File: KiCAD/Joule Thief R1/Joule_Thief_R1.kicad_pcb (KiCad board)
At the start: 2 copper layers, 95 x 62 mm, 35 parts, among them J2 Conn_01x06_Socket, Q1 AO3400A, Q2 AO3400A, SW1 SW_SPST, SW2 SW_SPST, U1 INA219AxD, U2 LTC3105xMS, U3 AD5280, U4 INA219AxD, U5 DW01A

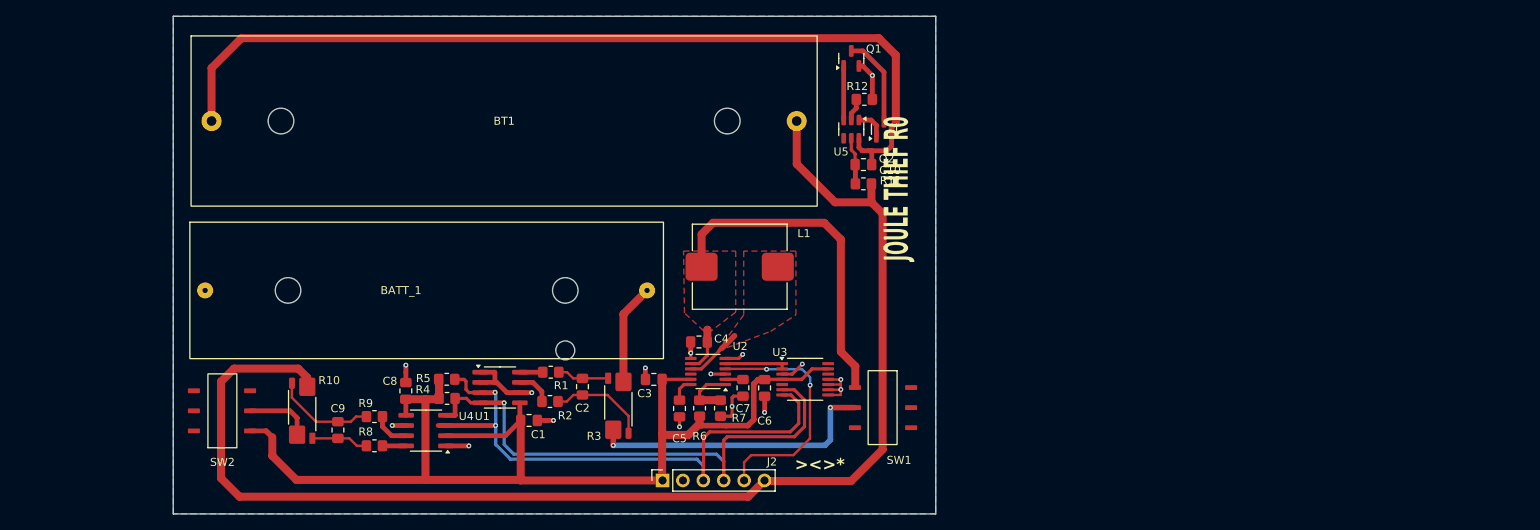
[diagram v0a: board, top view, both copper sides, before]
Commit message: layout extraction module
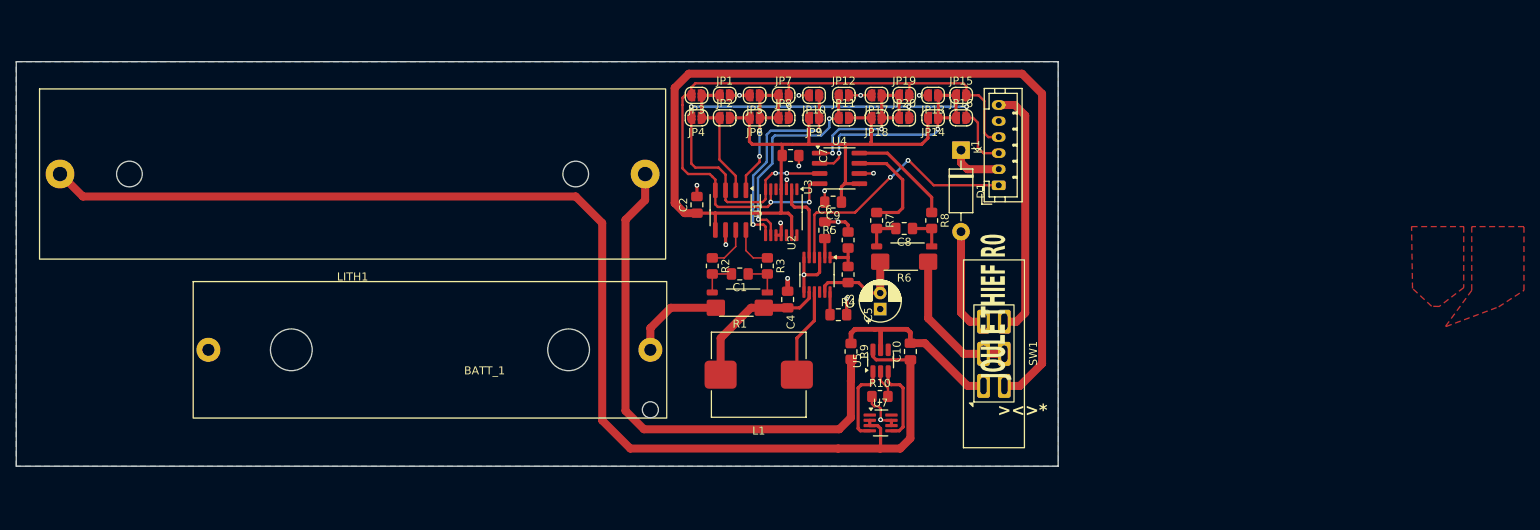
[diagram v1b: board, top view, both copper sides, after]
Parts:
- removed BT1: Battery_Cell, Joule Thief-Library:18650_Cell_Clip
- removed J2: Conn_01x06_Socket, Connector_PinSocket_2.54mm:PinSocket_1x06_P2.54mm_Vertical
- removed Q1, Q2: AO3400A, Package_TO_SOT_SMD:SOT-23
- removed R11: 100, Resistor_SMD:R_0805_2012Metric_Pad1.20x1.40mm_HandSolder
- removed R12: 1k, Resistor_SMD:R_0805_2012Metric_Pad1.20x1.40mm_HandSolder
- removed the R4 at (92.7, 77.0)
- removed the R5 at (92.7, 74.6)
- removed SW2: SW_SPST, Joule Thief-Library:SMD_DPST_Switch
- added D1: D_Schottky, Diode_THT:D_DO-41_SOD81_P10.16mm_Horizontal, F.Cu at (156.8, 46.0)
- added J1: Conn_01x06, Connector_JST:JST_PH_B6B-PH-K_1x06_P2.00mm_Vertical, F.Cu at (161.5, 50.4)
- added JP1: SolderJumper_2_Open, Jumper:SolderJumper-2_P1.3mm_Open_RoundedPad1.0x1.5mm, F.Cu at (127.3, 39.2)
- added JP10: SolderJumper_2_Open, Jumper:SolderJumper-2_P1.3mm_Open_RoundedPad1.0x1.5mm, F.Cu at (138.5, 39.2)
- added JP11: SolderJumper_2_Open, Jumper:SolderJumper-2_P1.3mm_Open_RoundedPad1.0x1.5mm, F.Cu at (142.2, 42.0)
- added JP12: SolderJumper_2_Open, Jumper:SolderJumper-2_P1.3mm_Open_RoundedPad1.0x1.5mm, F.Cu at (142.2, 39.2)
- added JP13: SolderJumper_2_Open, Jumper:SolderJumper-2_P1.3mm_Open_RoundedPad1.0x1.5mm, F.Cu at (153.3, 39.2)
- added JP14: SolderJumper_2_Open, Jumper:SolderJumper-2_P1.3mm_Open_RoundedPad1.0x1.5mm, F.Cu at (153.3, 42.0)
- added JP15: SolderJumper_2_Open, Jumper:SolderJumper-2_P1.3mm_Open_RoundedPad1.0x1.5mm, F.Cu at (156.8, 39.2)
- added JP16: SolderJumper_2_Open, Jumper:SolderJumper-2_P1.3mm_Open_RoundedPad1.0x1.5mm, F.Cu at (156.8, 42.0)
- added JP17: SolderJumper_2_Open, Jumper:SolderJumper-2_P1.3mm_Open_RoundedPad1.0x1.5mm, F.Cu at (146.2, 39.2)
- added JP18: SolderJumper_2_Open, Jumper:SolderJumper-2_P1.3mm_Open_RoundedPad1.0x1.5mm, F.Cu at (146.2, 42.0)
- added JP19: SolderJumper_2_Open, Jumper:SolderJumper-2_P1.3mm_Open_RoundedPad1.0x1.5mm, F.Cu at (149.7, 39.2)
- added JP2: SolderJumper_2_Open, Jumper:SolderJumper-2_P1.3mm_Open_RoundedPad1.0x1.5mm, F.Cu at (127.3, 42.0)
- added JP20: SolderJumper_2_Open, Jumper:SolderJumper-2_P1.3mm_Open_RoundedPad1.0x1.5mm, F.Cu at (149.7, 42.0)
- added JP3: SolderJumper_2_Open, Jumper:SolderJumper-2_P1.3mm_Open_RoundedPad1.0x1.5mm, F.Cu at (123.8, 39.2)
- added JP4: SolderJumper_2_Open, Jumper:SolderJumper-2_P1.3mm_Open_RoundedPad1.0x1.5mm, F.Cu at (123.8, 42.0)
- added JP5: SolderJumper_2_Open, Jumper:SolderJumper-2_P1.3mm_Open_RoundedPad1.0x1.5mm, F.Cu at (131.1, 39.2)
- added JP6: SolderJumper_2_Open, Jumper:SolderJumper-2_P1.3mm_Open_RoundedPad1.0x1.5mm, F.Cu at (131.1, 42.0)
- added JP7: SolderJumper_2_Open, Jumper:SolderJumper-2_P1.3mm_Open_RoundedPad1.0x1.5mm, F.Cu at (134.7, 39.2)
- added JP8: SolderJumper_2_Open, Jumper:SolderJumper-2_P1.3mm_Open_RoundedPad1.0x1.5mm, F.Cu at (134.7, 42.0)
- added JP9: SolderJumper_2_Open, Jumper:SolderJumper-2_P1.3mm_Open_RoundedPad1.0x1.5mm, F.Cu at (138.5, 42.0)
- added LITH1: 18650, 000_Dropbin:18650_Cell_Clip_V2, F.Cu at (81.0, 49.0)
- added R6: 0.1R, 000_Dropbin:R_Shunt_2512_V2, F.Cu at (149.7, 59.3)
- added R7: 10, Resistor_SMD:R_0805_2012Metric_Pad1.20x1.40mm_HandSolder, F.Cu at (146.3, 54.8)
- added U7: FS8205A, Package_TO_SOT_SMD:SOT-23-8_Handsoldering, F.Cu at (146.8, 80.0)
- BATT_1: footprint Joule Thief-Library:AA_Cell_Clip -> 000_Dropbin:AA_Cell_Clip_V2
- C3: footprint Capacitor_SMD:C_0805_2012Metric_Pad1.18x1.45mm_HandSolder -> Capacitor_THT:CP_Radial_D5.0mm_P2.00mm
- L1: footprint Joule Thief-Library:Power_Inductor_101040 -> 000_Dropbin:Power_Inductor_101040
- R1: value 10 -> 0.1R; footprint Resistor_SMD:R_0805_2012Metric_Pad1.20x1.40mm_HandSolder -> 000_Dropbin:R_Shunt_2512_V2
- R10: value 0.1R -> 1k; footprint Resistor_SMD:R_Shunt_Vishay_WSK2512_6332Metric_T1.19mm -> Resistor_SMD:R_0805_2012Metric_Pad1.20x1.40mm_HandSolder
- R3: value 0.1R -> 10; footprint Resistor_SMD:R_Shunt_Vishay_WSK2512_6332Metric_T1.19mm -> Resistor_SMD:R_0805_2012Metric_Pad1.20x1.40mm_HandSolder
- R4: renamed from R6; value 910k -> 1M
- R9: value 10 -> 100
- SW1: value SW_SPST -> SW_DPDT_x2; footprint Joule Thief-Library:SMD_DPST_Switch -> 000_Dropbin:SS22F25_DPDT_Straight_V2
- U5: value DW01A -> DW01; footprint Package_TO_SOT_SMD:SOT-23-6 -> Package_TO_SOT_SMD:SOT-23-6_Handsoldering
- moved R8 74.9 mm to (153.1, 54.8), turned to -90 degrees
- moved R10 72.0 mm to (146.7, 76.7), turned to 0 degrees
- moved C9 67.9 mm to (140.8, 52.5), turned to 180 degrees
- moved C8 65.3 mm to (149.7, 55.8), turned to 180 degrees
- moved U4 61.0 mm to (141.6, 48.3), turned to 0 degrees
- moved R9 59.9 mm to (143.1, 71.1), turned to -90 degrees
- moved U1 36.2 mm to (128.1, 53.5), turned to -90 degrees
- moved C1 32.0 mm to (129.2, 61.5), turned to 180 degrees
- moved C3 29.5 mm to (146.7, 65.8), turned to 90 degrees
- moved C7 29.1 mm to (135.5, 46.7), turned to 0 degrees
- moved U5 29.1 mm to (146.8, 72.2), turned to 90 degrees
- moved C2 26.8 mm to (123.9, 52.8), turned to 90 degrees
- moved R2 26.3 mm to (125.8, 60.5), turned to -90 degrees
- moved R5 26.3 mm to (142.7, 57.2), turned to 90 degrees
- moved R3 25.5 mm to (132.6, 60.5)
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- renumbered C7 to C6, C6 to C7, R7 to R5
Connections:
- BATT_1 pad 1: +ALK -> ALK
- C1 pad 1: V5+ -> Net-(C1-Pad1)
- C1 pad 2: GND -> Net-(C1-Pad2)
- C10 pad 1: Net-(U5-VCC) -> BAT-
- C10 pad 2: Net-(BT1--) -> Net-(SW1A-A)
- C2 pad 1: Net-(C2-Pad1) -> VBUS
- C2 pad 2: Net-(C2-Pad2) -> GND
- C3 pad 2: V5+ -> Net-(U2-VOUT)
- C4 pad 1: Net-(SW1-A) -> Net-(U2-VIN)
- C7 pad 1: V5+ -> VBUS
- C8 pad 1: V5+ -> Net-(C8-Pad1)
- C8 pad 2: GND -> Net-(C8-Pad2)
- C9 pad 1: Net-(C9-Pad1) -> VBUS
- C9 pad 2: Net-(C9-Pad2) -> GND
- L1 pad 1: Net-(SW1-A) -> Net-(U2-VIN)
- R1 pad 1: Net-(U1-IN+) -> Net-(U2-VIN)
- R1 pad 2: Net-(C2-Pad1) -> Net-(C1-Pad1)
- R10 pad 1: Net-(SW2-B) -> GND
- R10 pad 2: Net-(C9-Pad2) -> Net-(U5-CS)
- R2 pad 2: Net-(C2-Pad2) -> Net-(C1-Pad2)
- R3 pad 1: +ALK -> Net-(U1-IN+)
- R3 pad 2: Net-(C2-Pad1) -> Net-(C1-Pad1)
- R4 pad 1: V5+ -> Net-(U2-VOUT)
- R8 pad 2: Net-(C9-Pad2) -> Net-(C8-Pad1)
- R9 pad 1: Net-(U4-IN-) -> Net-(SW1A-A)
- R9 pad 2: Net-(C9-Pad1) -> BAT+
- SW1 pad 1: Net-(SW1-A) -> Net-(SW1A-A)
- SW1 pad 2: Net-(SW1-B) -> VBOOST
- SW1 pad 3: (no net) -> Net-(D1-A)
- SW1 pad 4: (no net) -> VBUS
- SW1 pad 5: (no net) -> VBOOST
- SW1 pad 6: (no net) -> VCC
- U1 pad 1: GND -> Net-(JP5-A)
- U1 pad 2: GND -> Net-(JP1-A)
- U1 pad 5: V5+ -> VBUS
- U2 pad 11: V5+ -> Net-(U2-VOUT)
- U2 pad 5: MPPC -> Net-(U2-MPPC)
- U2 pad 8: Net-(SW1-A) -> Net-(U2-VIN)
- U3 pad 1: MPPC -> unconnected-(U3-A-Pad1)
- U3 pad 13: V5+ -> VBUS
- U3 pad 2: MPPC -> Net-(U2-MPPC)
- U3 pad 4: V5+ -> VBUS
- U3 pad 8: GND -> Net-(JP10-A)
- U3 pad 9: GND -> Net-(JP11-A)
- U4 pad 1: GND -> Net-(JP17-A)
- U4 pad 2: V5+ -> Net-(JP13-A)
- U4 pad 5: V5+ -> VBUS
- U5 pad 5: Net-(U5-VCC) -> Net-(SW1A-A)
- U5 pad 6: Net-(BT1--) -> BAT-
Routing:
- net VBUS: track 0.00 -> 179.0 mm
- net LITH: track 161.2 -> 0.00 mm
- net BAT-: track 0.00 -> 155.0 mm
- net V5+: track 137.6 -> 0.00 mm
- net Net-(BT1--): track 113.2 -> 0.00 mm
- net BAT+: track 0.00 -> 67.7 mm
- net Net-(SW1-A): track 47.1 -> 0.00 mm
- net Net-(SW1-B): track 36.4 -> 0.00 mm, vias 2 -> 0
- net VCC: track 0.00 -> 31.5 mm
- net Net-(JP13-A): track 0.00 -> 29.8 mm, vias 0 -> 2
- net Net-(JP11-A): track 0.00 -> 26.8 mm, vias 0 -> 2
- net Net-(JP10-A): track 0.00 -> 25.7 mm, vias 0 -> 2
- net Net-(SW1A-A): track 0.00 -> 24.3 mm
- net Net-(JP17-A): track 0.00 -> 21.7 mm, vias 0 -> 2
- net Net-(JP5-A): track 0.00 -> 20.0 mm, vias 0 -> 2
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- added copper zone on F.Cu, net Net-(U2-VIN)
- removed copper zone on F.Cu, net Net-(SW1-A)
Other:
- board size 95 x 62 mm -> 129.8 x 50.4 mm
